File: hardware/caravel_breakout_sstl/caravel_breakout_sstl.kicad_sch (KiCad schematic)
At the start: 20 parts, among them J1 Conn_01x14_Female, J2 Conn_01x14_Female, J3 Conn_01x14_Female, J4 Conn_01x14_Female, T1 Logo, T2 Logo, U1 Caravel

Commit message: Finish first draft of schematic
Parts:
- removed J2: Conn_01x14_Female, Connector_PinHeader_1.27mm:PinHeader_2x14_P1.27mm_Vertical, symbol Connector:Conn_01x28_Female
- added C10: 10uf, Capacitor_SMD:C_0402_1005Metric, symbol Device:C
- added C11: 1uf, Capacitor_SMD:C_0402_1005Metric, symbol Device:C
- added C12: 0.1uf, Capacitor_SMD:C_0402_1005Metric, symbol Device:C
- added J2: Conn_Coaxial, symbol Connector:Conn_Coaxial
- added R1, R2, R3, R4: 75ohm, symbol Device:R_US
- added TP1, TP2, TP?: TestPoint, symbol Connector:TestPoint
- added U2: LTC1844ES5-1.5, Package_TO_SOT_SMD:TSOT-23-5, symbol custom_lib:LTC1844ES5-1.5
- added U3, U4: SN74AVC4T245PW, Package_SO:TSSOP-16_4.4x5mm_P0.65mm, symbol Logic_LevelTranslator:SN74AVC4T245PW
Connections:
- net dig_vdd is gone; now on net analog_vdd: U1.55 (mprj_io[18])
- net GND: now also C2.2, C3.2, J1.3 (Pin_3), J1.4 (Pin_4), C10.1, C11.1, C12.2, J2.2 (Ext), R2.1, R4.1, TP?.1, U2.2 (GND), U3.14 (2~{OE}), U3.15 (1~{OE}), U3.8 (GND), U3.9 (GND), U4.14 (2~{OE}), U4.15 (1~{OE}), U4.8 (GND), U4.9 (GND); no longer C2.1, C3.1
- net analog_vdd: now also C11.2, R1.1, R3.1, U2.5 (VOUT), U3.16 (VCCB), U4.16 (VCCB)
- net cfg_clk: now also U3.13 (1B1)
- net cfg_din: now also U3.12 (1B2)
- net prbs_clk_0: now also U4.13 (1B1)
- net prbs_clk_1: now also U4.12 (1B2)
- net prbs_clk_2: now also U4.11 (2B1)
- net tx_dq: now also R1.2, R2.2, TP1.1
- net vccd1: now also C2.1; no longer C2.2
- net vdda2: now also C3.1; no longer C3.2
- net ~{prbs_rst}: now also U4.10 (2B2)
- net ~{tx_dq}: now also R3.2, R4.2, TP2.1
- net vin_3v3: now reaches J1.1 (Pin_1)
- net vin_3v3: now also J1.2 (Pin_2), C10.2, U2.1 (~{SHDN}), U2.4 (VIN), U3.1 (VCCA), U3.2 (1DIR), U3.3 (2DIR), U4.1 (VCCA), U4.2 (1DIR), U4.3 (2DIR)
- net cfg_clk_vin: now reaches J1.17 (Pin_17)
- net cfg_clk_vin: now also J1.18 (Pin_18), U3.4 (1A1)
- net cfg_din_vin: now reaches J1.19 (Pin_19)
- net cfg_din_vin: now also J1.20 (Pin_20), U3.5 (1A2)
- net prbs_clk_0_vin: now reaches J1.21 (Pin_21)
- net prbs_clk_0_vin: now also J1.22 (Pin_22), U4.4 (1A1)
- net prbs_clk_1_vin: now reaches J1.23 (Pin_23)
- net prbs_clk_1_vin: now also J1.24 (Pin_24), U4.5 (1A2)
- net prbs_clk_2_vin: now reaches J1.25 (Pin_25)
- net prbs_clk_2_vin: now also J1.26 (Pin_26), U4.6 (2A1)
- net ~{prsb_rst_vin}: now reaches J1.27 (Pin_27)
- net ~{prsb_rst_vin}: now also J1.28 (Pin_28), U4.7 (2A2)
- net rx_dq: no longer names the net of U1.62 (mprj_io[24])
- net rx_dq: now also J2.1 (In)
- new net: C12.1, U2.3 (BYP)
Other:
- company: (none) -> University of Washington Department of Computer Science and Engineering
- title: (none) -> Caravan SSTL Test Board
- moved on the sheet: C2, C3, H1, H2, H3, H4, J1, J3, J4, T1, T2

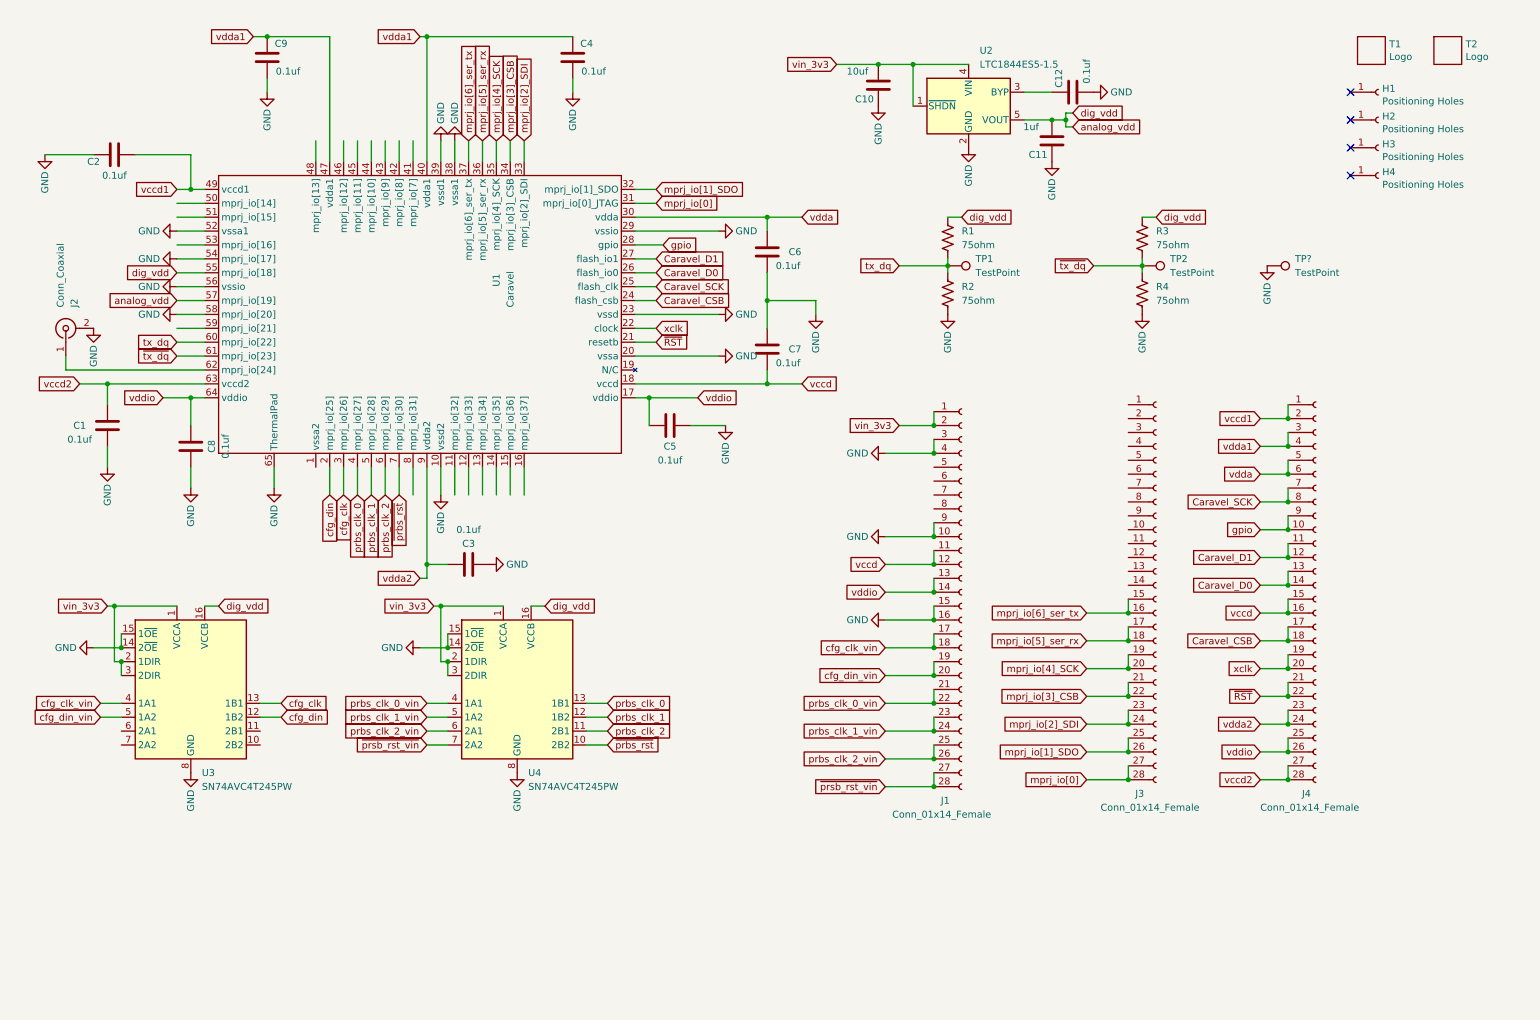
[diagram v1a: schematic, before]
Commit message: Update schematic
* Add new connectors
* Add some caps
* Add alternate power jumper
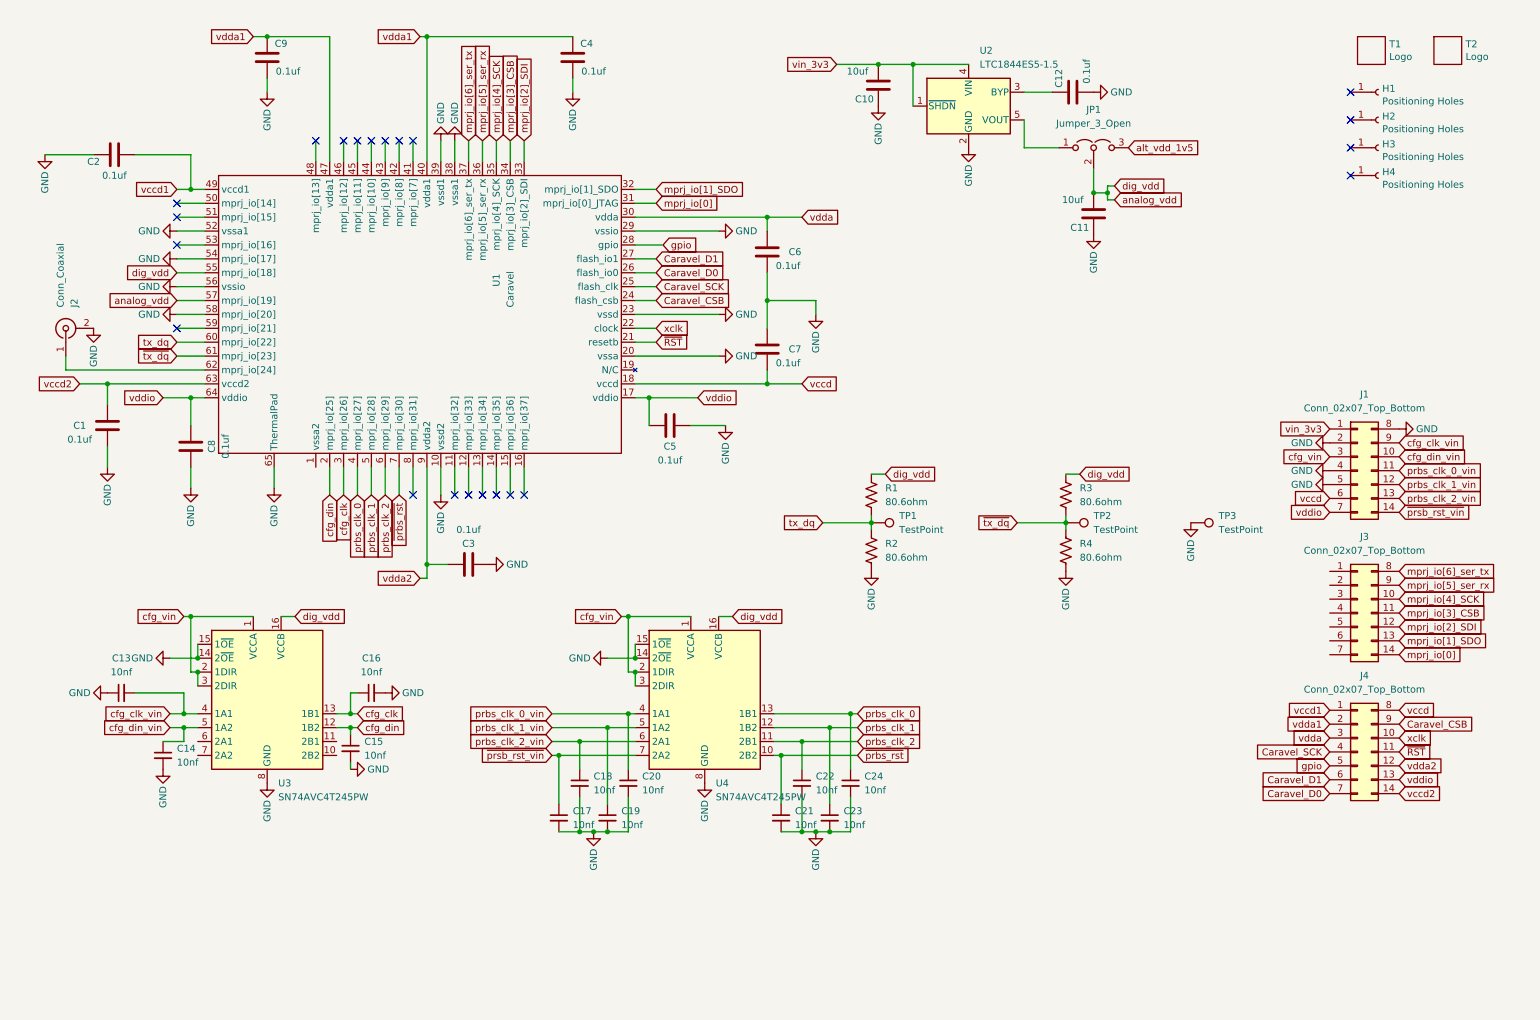
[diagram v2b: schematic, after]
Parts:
- removed J1, J3, J4: Conn_01x14_Female, Connector_PinHeader_1.27mm:PinHeader_2x14_P1.27mm_Vertical, symbol Connector:Conn_01x28_Female
- added C13, C14, C15, C16, C17, C18, C19, C20, C21, C22, C23, C24: 10nf, symbol Device:C_Small
- added J1, J3, J4: Conn_02x07_Top_Bottom, symbol Connector_Generic:Conn_02x07_Top_Bottom
- added JP1: Jumper_3_Open, symbol Jumper:Jumper_3_Open
- C11: value 1uf -> 10uf
- R1, R2, R3, R4: value 75ohm -> 80.6ohm
- gave numbers to parts that had none: 1
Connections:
- net Caravel_CSB: now also J4.9 (Pin_9)
- net Caravel_D0: now also J4.7 (Pin_7)
- net Caravel_D1: now also J4.6 (Pin_6)
- net Caravel_SCK: now also J4.4 (Pin_4)
- net GND: now also R2.2, R4.2, C13.1, C14.2, C15.2, C16.2, C17.2, C18.2, C19.2, C20.2, C21.2, C22.2, C23.2, C24.2, J1.2 (Pin_2), J1.4 (Pin_4), J1.5 (Pin_5), J1.8 (Pin_8); no longer R2.1, R4.1
- net analog_vdd: now also JP1.2 (C); no longer U2.5 (VOUT)
- net cfg_clk: now also C16.1
- net cfg_clk_vin: now also C13.2, J1.9 (Pin_9)
- net cfg_din: now also C15.1
- net cfg_din_vin: now also C14.1, J1.10 (Pin_10)
- net gpio: now also J4.5 (Pin_5)
- net mprj_io[0]: now also J3.14 (Pin_14)
- net mprj_io[1]_SDO: now also J3.13 (Pin_13)
- net mprj_io[2]_SDI: now also J3.12 (Pin_12)
- net mprj_io[3]_CSB: now also J3.11 (Pin_11)
- net mprj_io[4]_SCK: now also J3.10 (Pin_10)
- net mprj_io[5]_ser_rx: now also J3.9 (Pin_9)
- net mprj_io[6]_ser_tx: now also J3.8 (Pin_8)
- net prbs_clk_0: now also C24.1
- net prbs_clk_0_vin: now also C20.1, J1.11 (Pin_11)
- net prbs_clk_1: now also C23.1
- net prbs_clk_1_vin: now also C19.1, J1.12 (Pin_12)
- net prbs_clk_2: now also C22.1
- net prbs_clk_2_vin: now also C18.1, J1.13 (Pin_13)
- net tx_dq: now also R2.1; no longer R2.2
- net vccd: now also J1.6 (Pin_6), J4.8 (Pin_8)
- net vccd1: now also J4.1 (Pin_1)
- net vccd2: now also J4.14 (Pin_14)
- net vdda: now also J4.3 (Pin_3)
- net vdda1: now also J4.2 (Pin_2)
- net vdda2: now also J4.12 (Pin_12)
- net vddio: now also J1.7 (Pin_7), J4.13 (Pin_13)
- net vin_3v3: now also J1.1 (Pin_1); no longer U3.1 (VCCA), U3.2 (1DIR), U3.3 (2DIR), U4.1 (VCCA), U4.2 (1DIR), U4.3 (2DIR)
- net xclk: now also J4.10 (Pin_10)
- net ~{RST}: now also J4.11 (Pin_11)
- net ~{prbs_rst}: now also C21.1
- net ~{prsb_rst_vin}: now also C17.1, J1.14 (Pin_14)
- net ~{tx_dq}: now also R4.1; no longer R4.2
- new net: JP1.1 (A), U2.5 (VOUT)
- new net alt_vdd_1v5: JP1.3 (B)
- new net cfg_vin: J1.3 (Pin_3), U3.1 (VCCA), U3.2 (1DIR), U3.3 (2DIR), U4.1 (VCCA), U4.2 (1DIR), U4.3 (2DIR)
- no-connect marks 4 -> 22
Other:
- moved on the sheet: C11, R1, TP1, TP2, TP3, U3, U4

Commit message: Minor fixes
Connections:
- net GND: no longer J1.2 (Pin_2)
- net alt_vdd_1v5: now also J1.2 (Pin_2)
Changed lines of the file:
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@@
+    )
+  )
+  (global_label "alt_vdd_1v5" (shape input) (at 252.73 93.345 180) (fields_autoplaced)
+    (effects (font (size 1.27 1.27)) (justify right))
+    (property "Intersheet References" "${INTERSHEET_REFS}" (id 0) (at 239.1893 93.4244 0)
+      (effects (font (size 1.27 1.27)) (justify right) hide)
     )
   )
@@
     (pin "2")
   )
-  (symbol (lib_id "power:GND") (at 252.73 93.345 270) (mirror x) (unit 1)
-    (in_bom yes) (on_board yes)
-    (property "Reference" "#PWR040" (id 0) (at 246.38 93.345 0)
-      (effects (font (size 1.27 1.27)) hide)
-    )
-    (property "Value" "GND" (id 1) (at 247.65 93.345 90))
-    (property "Footprint" "" (id 2) (at 252.73 93.345 0)
-      (effects (font (size 1.27 1.27)) hide)
-    )
-    (property "Datasheet" "" (id 3) (at 252.73 93.345 0)
-      (effects (font (size 1.27 1.27)) hide)
-    )
-    (pin "1")
-  )
   (symbol (lib_id "Logic_LevelTranslator:SN74AVC4T245PW") (at 138.43 140.335 0) (unit 1)
     (in_bom yes) (on_board yes) (fields_autoplaced)
@@
       (reference "#PWR039") (unit 1) (value "GND") (footprint "")
     )
-    (path "/f106dc71-f35d-4bde-bcea-6321a9a96054"
-      (reference "#PWR040") (unit 1) (value "GND") (footprint "")
-    )
     (path "/4ca28c28-ea0f-4fdd-9d07-75b7f20ec282"

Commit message: Finish draft of Layout
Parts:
- removed C13, C14, C15, C16, C17, C18, C19, C20, C21, C22, C23, C24: 10nf, symbol Device:C_Small
- removed H1, H2, H3, H4: Positioning Holes, MountingHole:MountingHole_2.2mm_M2_ISO7380_Pad, symbol Connector:Conn_01x01_Female
- removed TP1, TP2, TP3: TestPoint, symbol Connector:TestPoint
- added C13, C14, C15, C16: 0.1uf, Capacitor_SMD:C_0402_1005Metric, symbol Device:C
- added TP1, TP2: TestPoint_2Pole, TestPoint:TestPoint_2Pads_Pitch2.54mm_Drill0.8mm, symbol Connector:TestPoint_2Pole
- C10, C11: footprint Capacitor_SMD:C_0402_1005Metric -> Capacitor_SMD:C_0805_2012Metric
- J1, J3, J4: footprint (none) -> Connector_PinSocket_2.54mm:PinSocket_2x07_P2.54mm_Vertical; symbol Connector_Generic:Conn_02x07_Top_Bottom -> Connector_Generic:Conn_02x07_Odd_Even
- J2: footprint (none) -> Connector_Coaxial:SMA_Amphenol_132134-16_Vertical
- JP1: footprint (none) -> Connector_PinHeader_2.54mm:PinHeader_1x03_P2.54mm_Vertical
- R1, R2, R3, R4: footprint (none) -> Resistor_SMD:R_0402_1005Metric
- U3, U4: footprint Package_SO:TSSOP-16_4.4x5mm_P0.65mm -> custom_footprints:Texas_R-PDSO-G16
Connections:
- net Caravel_CSB: now also J4.7 (Pin_7); no longer J4.9 (Pin_9)
- net Caravel_D0: now also J4.5 (Pin_5); no longer J4.7 (Pin_7)
- net Caravel_SCK: now also J4.8 (Pin_8); no longer J4.4 (Pin_4)
- net GND: now also C2.1, J1.2 (Pin_2), J1.7 (Pin_7), J1.9 (Pin_9), U1.1 (vssa2), C13.1, C14.1, C15.1, C16.1, TP1.2, TP2.2; no longer C2.2, J1.4 (Pin_4), J1.5 (Pin_5), J1.8 (Pin_8)
- net alt_vdd_1v5: now also J1.3 (Pin_3); no longer J1.2 (Pin_2)
- net analog_vdd: now also C14.2, C16.2; no longer C11.2
- net cfg_clk_vin: now also J1.4 (Pin_4); no longer J1.9 (Pin_9)
- net cfg_din_vin: now also J1.6 (Pin_6); no longer J1.10 (Pin_10)
- net cfg_vin: now also J1.5 (Pin_5), C13.2, C15.2; no longer J1.3 (Pin_3)
- net gpio: now also J4.3 (Pin_3); no longer J4.5 (Pin_5)
- net mprj_io[1]_SDO: now also J3.12 (Pin_12); no longer J3.13 (Pin_13)
- net mprj_io[2]_SDI: now also J3.10 (Pin_10); no longer J3.12 (Pin_12)
- net mprj_io[3]_CSB: now also J3.8 (Pin_8); no longer J3.11 (Pin_11)
- net mprj_io[4]_SCK: now also J3.6 (Pin_6); no longer J3.10 (Pin_10)
- net mprj_io[5]_ser_rx: now also J3.4 (Pin_4); no longer J3.9 (Pin_9)
- net mprj_io[6]_ser_tx: now also J3.2 (Pin_2); no longer J3.8 (Pin_8)
- net prbs_clk_0_vin: now also J1.8 (Pin_8); no longer J1.11 (Pin_11)
- net prbs_clk_1_vin: now also J1.10 (Pin_10); no longer J1.12 (Pin_12)
- net prbs_clk_2_vin: now also J1.12 (Pin_12); no longer J1.13 (Pin_13)
- net tx_dq: now also TP1.1
- net vccd: now also J1.11 (Pin_11), J4.10 (Pin_10); no longer J1.6 (Pin_6), J4.8 (Pin_8)
- net vccd1: now also C2.2; no longer C2.1
- net vdda: now also J4.4 (Pin_4); no longer J4.3 (Pin_3)
- net vdda2: now also J4.11 (Pin_11); no longer J4.12 (Pin_12)
- net vddio: now also J1.13 (Pin_13), J4.12 (Pin_12); no longer J1.7 (Pin_7), J4.13 (Pin_13)
- net vin_3v3: now also U2.3 (~{SHDN}); no longer U2.4 (VIN)
- net xclk: now also J4.9 (Pin_9); no longer J4.10 (Pin_10)
- net ~{RST}: now also J4.13 (Pin_13); no longer J4.11 (Pin_11)
- net ~{tx_dq}: now also TP2.1
- net at JP1.1 (A), U2.5 (VOUT): now also C11.2
- net at C12.1: now also U2.4 (BYP); no longer U2.3 (BYP)
- no-connect marks 22 -> 29
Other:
- moved on the sheet: C2, R1, R2, R3, R4
